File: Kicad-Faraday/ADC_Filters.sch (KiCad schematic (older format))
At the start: 14 parts

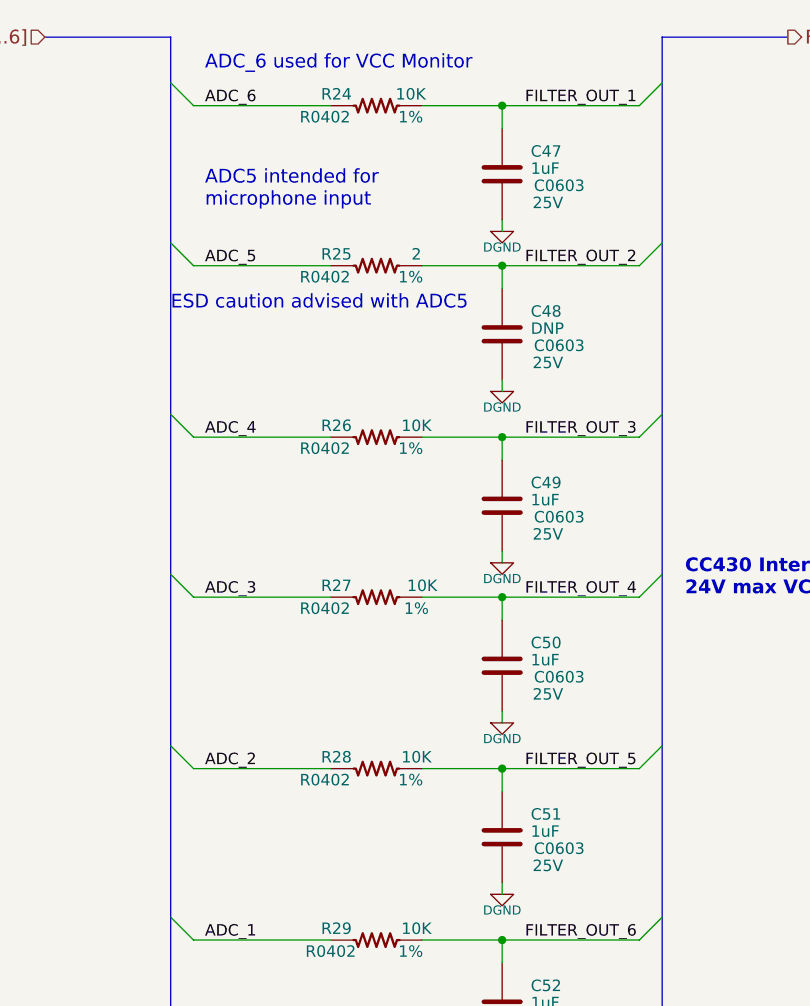
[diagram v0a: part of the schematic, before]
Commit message: Updated per RevD Github Issue comments. Largely removed unnecessary items
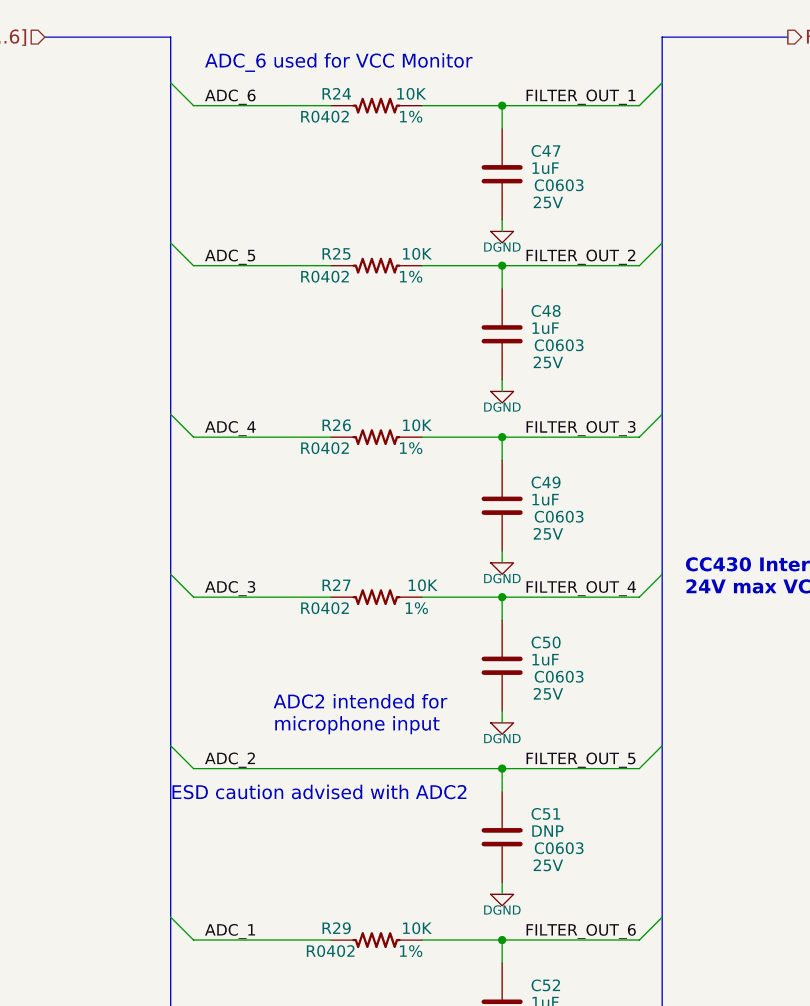
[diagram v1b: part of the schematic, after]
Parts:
- removed R28: 10K, R0402, symbol R_US
- C48: value DNP -> 1uF
- C51: value 1uF -> DNP
- R25: value 2 -> 10K
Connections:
- net FILTER_OUT_5 is gone; now on net ADC_2: C51.1
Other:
- note added: "ADC2 intended for\nmicrophone input"
- note added: "ESD caution advised with ADC2"
- note removed: "ADC5 intended for\nmicrophone input"
- note removed: "ESD caution advised with ADC5"
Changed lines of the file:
@@
 Sheet 4 11
 Title "Faraday Wireless Node"
-Date "24 oct 2016"
+Date "10 nov 2016"
 Rev "C"
 Comp "FaradayRF"
@@
 P 8600 4350
 F 0 "R25" V 8650 4525 50  0000 C CNN
-F 1 "2" V 8650 4175 50  0000 C CNN
+F 1 "10K" V 8650 4175 50  0000 C CNN
 F 2 "R0402" V 8550 4575 50  0000 C CNN
 F 3 "" H 8600 4350 60  0000 C CNN
@@
 P 9150 4650
 F 0 "C48" H 9275 4750 50  0000 L CNN
-F 1 "DNP" H 9275 4675 50  0000 L CNN
+F 1 "1uF" H 9275 4675 50  0000 L CNN
 F 2 "C0603" H 9400 4600 50  0000 C CNN
 F 3 "" H 9150 4650 60  0000 C CNN
@@
 $EndComp
 $Comp
-L R_US R28
-U 1 1 54F7059B
-P 8600 6550
-F 0 "R28" V 8650 6725 50  0000 C CNN
-F 1 "10K" V 8650 6375 50  0000 C CNN
-F 2 "R0402" V 8550 6775 50  0000 C CNN
-F 3 "" H 8600 6550 60  0000 C CNN
-F 4 "1%" V 8550 6400 50  0000 C CNN "Tolerance"
-	1    8600 6550
-	0    -1   -1   0
-$EndComp
-$Comp
 L C C51
 U 1 1 54F705A1
 P 9150 6850
 F 0 "C51" H 9275 6950 50  0000 L CNN
-F 1 "1uF" H 9275 6875 50  0000 L CNN
+F 1 "DNP" H 9275 6875 50  0000 L CNN
 F 2 "C0603" H 9400 6800 50  0000 C CNN
 F 3 "" H 9150 6850 60  0000 C CNN
@@
 	7800 5800 8400 5800
 Wire Wire Line
-	7800 6550 8400 6550
+	7800 6550 9750 6550
 Wire Wire Line
 	7800 7300 8400 7300
@@
 Wire Wire Line
 	9150 6650 9150 6550
-Wire Wire Line
-	8800 6550 9750 6550
 Wire Wire Line
 	9150 6300 9150 6350
@@
 Connection ~ 9150 3650
 $Comp
-L DGND #PWR052
+L DGND #PWR046
 U 1 1 55BDE2A7
 P 9150 4200
-F 0 "#PWR052" H 9150 4200 40  0001 C CNN
+F 0 "#PWR046" H 9150 4200 40  0001 C CNN
 F 1 "DGND" H 9150 4130 40  0000 C CNN
 F 2 "~" H 9150 4200 60  0000 C CNN
@@
 $EndComp
 $Comp
-L DGND #PWR053
+L DGND #PWR047
 U 1 1 55BDE2AD
 P 9150 4900
-F 0 "#PWR053" H 9150 4900 40  0001 C CNN
+F 0 "#PWR047" H 9150 4900 40  0001 C CNN
 F 1 "DGND" H 9150 4830 40  0000 C CNN
 F 2 "~" H 9150 4900 60  0000 C CNN
@@
 $EndComp
 $Comp
-L DGND #PWR054
+L DGND #PWR048
 U 1 1 55BDE2B3
 P 9150 5650
-F 0 "#PWR054" H 9150 5650 40  0001 C CNN
+F 0 "#PWR048" H 9150 5650 40  0001 C CNN
 F 1 "DGND" H 9150 5580 40  0000 C CNN
 F 2 "~" H 9150 5650 60  0000 C CNN
@@
 $EndComp
 $Comp
-L DGND #PWR055
+L DGND #PWR049
 U 1 1 55BDE2B9
 P 9150 6350
-F 0 "#PWR055" H 9150 6350 40  0001 C CNN
+F 0 "#PWR049" H 9150 6350 40  0001 C CNN
 F 1 "DGND" H 9150 6280 40  0000 C CNN
 F 2 "~" H 9150 6350 60  0000 C CNN
@@
 $EndComp
 $Comp
-L DGND #PWR056
+L DGND #PWR050
 U 1 1 55BDE2BF
 P 9150 7100
-F 0 "#PWR056" H 9150 7100 40  0001 C CNN
+F 0 "#PWR050" H 9150 7100 40  0001 C CNN
 F 1 "DGND" H 9150 7030 40  0000 C CNN
 F 2 "~" H 9150 7100 60  0000 C CNN
@@
 $EndComp
 $Comp
-L DGND #PWR057
+L DGND #PWR051
 U 1 1 55BDE2C5
 P 9150 7850
-F 0 "#PWR057" H 9150 7850 40  0001 C CNN
+F 0 "#PWR051" H 9150 7850 40  0001 C CNN
 F 1 "DGND" H 9150 7780 40  0000 C CNN
 F 2 "~" H 9150 7850 60  0000 C CNN
@@
 $EndComp
 $Comp
-L DGND #PWR058
+L DGND #PWR052
 U 1 1 55BDE2CB
 P 9150 8650
-F 0 "#PWR058" H 9150 8650 40  0001 C CNN
+F 0 "#PWR052" H 9150 8650 40  0001 C CNN
 F 1 "DGND" H 9150 8580 40  0000 C CNN
 F 2 "~" H 9150 8650 60  0000 C CNN
@@
 Wire Wire Line
 	9150 8600 9150 8650
-Text Notes 7850 4100 0    60   ~ 0
-ADC5 intended for\nmicrophone input
-Text Notes 7700 4550 0    60   ~ 0
-ESD caution advised with ADC5
+Text Notes 8150 6400 0    60   ~ 0
+ADC2 intended for\nmicrophone input
+Text Notes 7700 6700 0    60   ~ 0
+ESD caution advised with ADC2
 $EndSCHEMATC

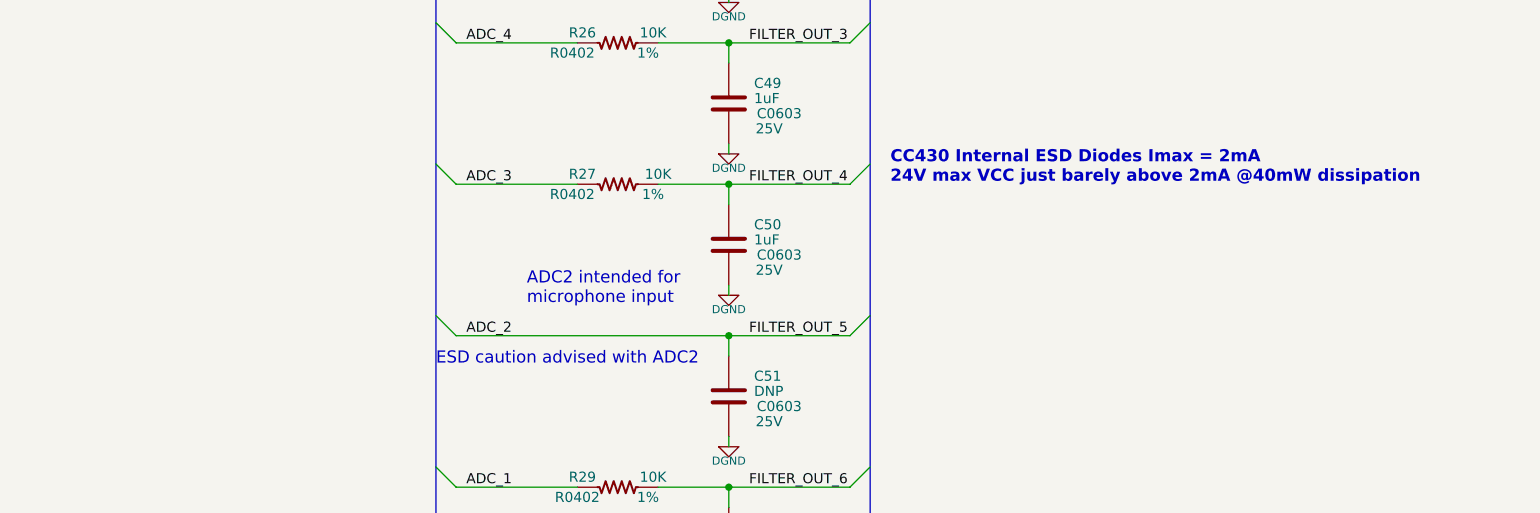
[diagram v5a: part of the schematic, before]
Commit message: Removed old rev c zip fabrication file. Created new gerbers and a new Rev d fabrication zip file. Also combined NPTH and plated TH drill files into faraday-all.drl. Updated read.me in fab zip file to summarize the new combined drill file. Advanced Circuits freedfm seems to have passed!
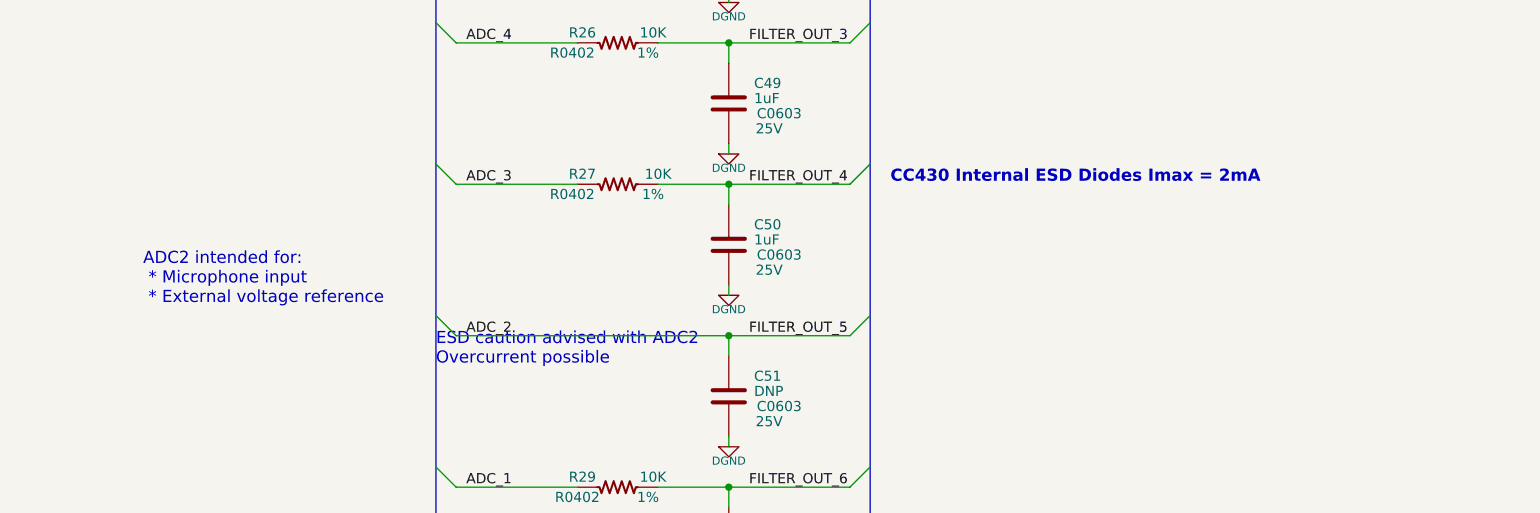
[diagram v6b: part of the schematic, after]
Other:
- note added: "ADC2 intended for:\n * Microphone input\n * External voltage reference"
- note added: "CC430 Internal ESD Diodes Imax = 2mA"
- note added: "ESD caution advised with ADC2\nOvercurrent possible"
- note removed: "ADC2 intended for\nmicrophone input"
- note removed: "CC430 Internal ESD Diodes Imax = 2mA\n24V max VCC just barely above 2mA @40mW dissipation"
- note removed: "ESD caution advised with ADC2"
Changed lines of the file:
@@
 Sheet 4 11
 Title "Faraday Wireless Node"
-Date "15 nov 2016"
+Date "16 nov 2016"
 Rev "D1"
 Comp "FaradayRF"
@@
 16 Hz ADC Filters
 Text Notes 9950 5800 0    60   ~ 12
-CC430 Internal ESD Diodes Imax = 2mA\n24V max VCC just barely above 2mA @40mW dissipation
+CC430 Internal ESD Diodes Imax = 2mA
 Text Notes 7975 2725 0    60   ~ 0
 Filter channels flipped for routing!
@@
 Wire Wire Line
 	9150 8600 9150 8650
-Text Notes 8150 6400 0    60   ~ 0
-ADC2 intended for\nmicrophone input
+Text Notes 6250 6400 0    60   ~ 0
+ADC2 intended for:\n * Microphone input\n * External voltage reference
 Text Notes 7700 6700 0    60   ~ 0
-ESD caution advised with ADC2
+ESD caution advised with ADC2\nOvercurrent possible
 $EndSCHEMATC
